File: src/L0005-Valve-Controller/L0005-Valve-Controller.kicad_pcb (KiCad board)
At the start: 4 copper layers, 141.7 x 50.5 mm, 100 parts, among them J1 Jumper_NO, J2 Jumper_NO, K1 AQH0223AX, K2 AQH0223AX, K3 AQH0223AX, K4 AQH0223AX, K5 AQH0223AX, K6 AQH0223AX, P1 3220-20-0200-00, P10 353620650, P11 353620650, P12 353620650, P13 353620650, P14 647676-3, P15 647676-3, P16 647676-2, P2 140-504-415-000, P3 647676-3, P4 647676-3, P5 647676-3, P6 647676-3, P7 647676-3, P8 647676-3, P9 647676-2, U1 LPC54113J256BD64QL, U2 LMS8117AMP-3.3_NOPB, U3 MAX3370EXK+T, U4 MAX3370EXK+T, U5 Optocoupler

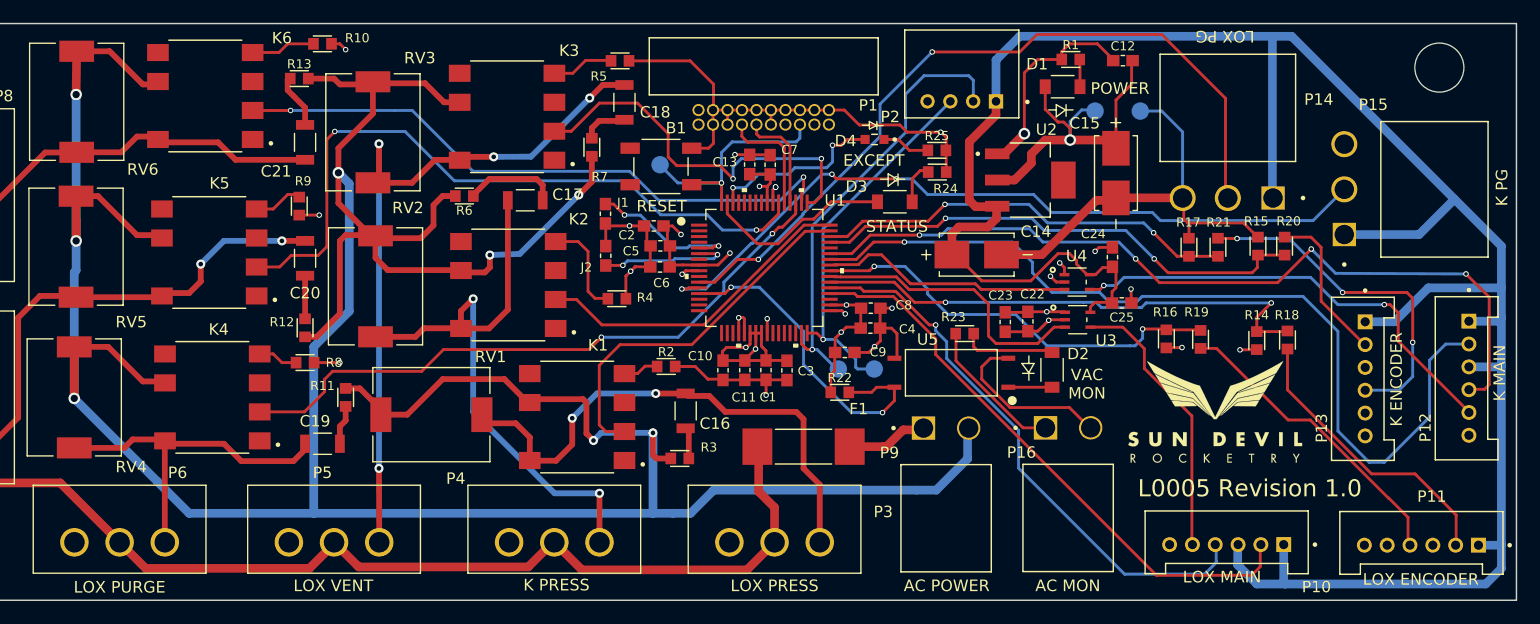
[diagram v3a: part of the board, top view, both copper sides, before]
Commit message: rerouted PCB to include 5V logic MOSFETS
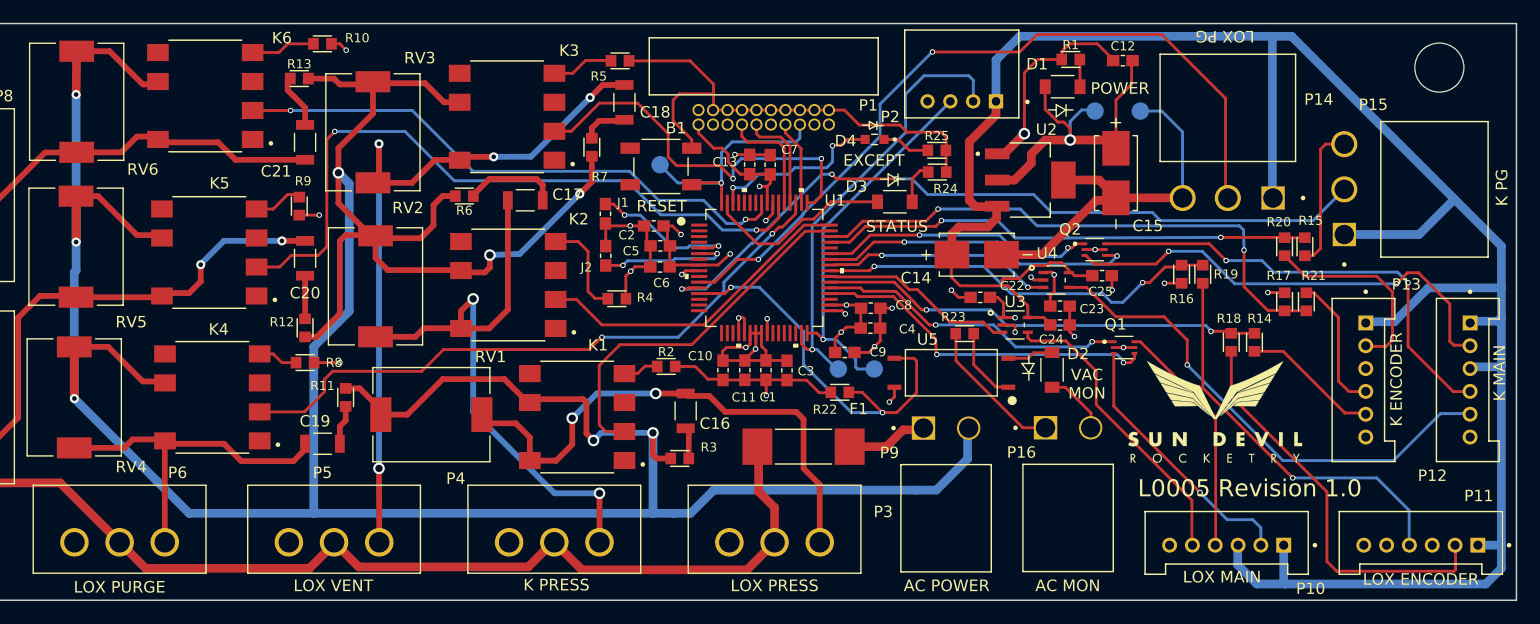
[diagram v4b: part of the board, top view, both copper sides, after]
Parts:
- added Q1: CMLDM7003, L0005-Valve-Controller:CMLDM7003 TR, F.Cu at (164.2, 105.4)
- added Q2: CMLDM7003, L0005-Valve-Controller:CMLDM7003 TR, F.Cu at (161.7, 96.8)
- B1: value PTS647SM38SMTR2LFS -> SW_PTS647SM38SMTR2LFS_CNK
- C14, C15: footprint Engine-Controller:CWR11HH106KB -> L0005-Valve-Controller:CWR11HH106KB
- LOGO1: value Logo -> LOGO
- U1: value LPC54113J256BD64QL -> LQFP64_10X10_NXP
- moved R17 9.65 mm to (178.3, 101.3)
- moved R21 9.10 mm to (180.2, 101.3)
- moved C24 7.51 mm to (158.6, 103.4), turned to 180 degrees
- moved R16 5.82 mm to (169.3, 98.9)
- moved R19 5.72 mm to (171.1, 98.9)
- moved U3 5.51 mm to (154.7, 103.4)
- moved C23 5.00 mm to (158.6, 101.7), turned to 180 degrees
- moved R18 4.93 mm to (173.6, 104.9)
- moved C22 4.67 mm to (151.6, 101.0), turned to 0 degrees
- moved R15 4.12 mm to (180.1, 96.5), turned to -90 degrees
- moved C25 2.95 mm to (162.3, 99.1)
- moved U4 1.85 mm to (158.3, 99.4)
- moved R14 0.25 mm to (175.7, 104.9)
- moved P12 0.18 mm to (194.6, 108.2)
- moved P13 0.11 mm to (185.4, 108.2)
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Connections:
- net /SBV1_PUL5 renamed /Valves/SBV1_PUL5
- net /SBV2_PUL5 renamed /Valves/SBV2_PUL5
- B1 pad 2: Net-(B1-Pad2) -> unconnected-(B1-Pad2)
- B1 pad 4: Net-(B1-Pad4) -> unconnected-(B1-Pad4)
- K1 pad 1: Net-(K1-Pad1) -> unconnected-(K1-Pad1)
- K1 pad 3: Net-(K1-Pad3) -> unconnected-(K1-Pad3)
- K1 pad 5: Net-(K1-Pad5) -> unconnected-(K1-Pad5)
- K2 pad 1: Net-(K2-Pad1) -> unconnected-(K2-Pad1)
- K2 pad 3: Net-(K2-Pad3) -> unconnected-(K2-Pad3)
- K2 pad 5: Net-(K2-Pad5) -> unconnected-(K2-Pad5)
- K3 pad 1: Net-(K3-Pad1) -> unconnected-(K3-Pad1)
- K3 pad 3: Net-(K3-Pad3) -> unconnected-(K3-Pad3)
- K3 pad 5: Net-(K3-Pad5) -> unconnected-(K3-Pad5)
- K4 pad 1: Net-(K4-Pad1) -> unconnected-(K4-Pad1)
- K4 pad 3: Net-(K4-Pad3) -> unconnected-(K4-Pad3)
- K4 pad 5: Net-(K4-Pad5) -> unconnected-(K4-Pad5)
- K5 pad 1: Net-(K5-Pad1) -> unconnected-(K5-Pad1)
- K5 pad 3: Net-(K5-Pad3) -> unconnected-(K5-Pad3)
- K5 pad 5: Net-(K5-Pad5) -> unconnected-(K5-Pad5)
- K6 pad 1: Net-(K6-Pad1) -> unconnected-(K6-Pad1)
- K6 pad 3: Net-(K6-Pad3) -> unconnected-(K6-Pad3)
- K6 pad 5: Net-(K6-Pad5) -> unconnected-(K6-Pad5)
- P1 pad 11: Earth -> unconnected-(P1-Pad11)
- P1 pad 13: Net-(P1-Pad13) -> SWO
- P1 pad 17: Net-(P1-Pad17) -> unconnected-(P1-Pad17)
- P1 pad 19: Net-(P1-Pad19) -> unconnected-(P1-Pad19)
- P1 pad 2: 3.3V -> unconnected-(P1-Pad2)
- P1 pad 3: Earth -> unconnected-(P1-Pad3)
- P1 pad 5: Earth -> unconnected-(P1-Pad5)
- P10 pad 2: ~{SBV1_EN} -> Net-(P10-Pad2)
- P10 pad 4: ~{SBV1_DIR} -> Net-(P10-Pad4)
- P12 pad 2: ~{SBV2_EN} -> Net-(P12-Pad2)
- P12 pad 4: ~{SBV2_DIR} -> Net-(P12-Pad4)
- P16 pad 2: Net-(P16-Pad2) -> Net-(D2-Pad1)
- P3 pad 3: Net-(P3-Pad3) -> unconnected-(P3-Pad3)
- P4 pad 3: Net-(P4-Pad3) -> unconnected-(P4-Pad3)
- P5 pad 3: Net-(P5-Pad3) -> unconnected-(P5-Pad3)
- P6 pad 3: Net-(P6-Pad3) -> unconnected-(P6-Pad3)
- P7 pad 3: Net-(P7-Pad3) -> unconnected-(P7-Pad3)
- P8 pad 3: Net-(P8-Pad3) -> unconnected-(P8-Pad3)
- R22 pad 1: 3.3V -> VAC_MON
- R22 pad 2: VAC_MON -> Earth
- R23 pad 1: Net-(D2-Pad2) -> Net-(R23-Pad1)
- U1 pad 1: Net-(U1-Pad1) -> unconnected-(U1-Pad1)
- U1 pad 10: Net-(U1-Pad10) -> unconnected-(U1-Pad10)
- U1 pad 14: Net-(U1-Pad14) -> unconnected-(U1-Pad14)
- U1 pad 15: Net-(U1-Pad15) -> unconnected-(U1-Pad15)
- U1 pad 16: Net-(U1-Pad16) -> unconnected-(U1-Pad16)
- U1 pad 17: Net-(U1-Pad17) -> unconnected-(U1-Pad17)
- U1 pad 18: Net-(U1-Pad18) -> unconnected-(U1-Pad18)
- U1 pad 19: Net-(U1-Pad19) -> unconnected-(U1-Pad19)
- U1 pad 2: Net-(U1-Pad2) -> unconnected-(U1-Pad2)
- U1 pad 26: Net-(U1-Pad26) -> unconnected-(U1-Pad26)
- U1 pad 27: Net-(U1-Pad27) -> unconnected-(U1-Pad27)
- U1 pad 28: Net-(U1-Pad28) -> unconnected-(U1-Pad28)
- U1 pad 29: Net-(U1-Pad29) -> unconnected-(U1-Pad29)
- U1 pad 3: Net-(U1-Pad3) -> unconnected-(U1-Pad3)
- U1 pad 30: Net-(U1-Pad30) -> unconnected-(U1-Pad30)
- U1 pad 35: Net-(U1-Pad35) -> unconnected-(U1-Pad35)
- U1 pad 36: ~{SBV1_EN} -> SBV1_EN
- U1 pad 37: ~{SBV1_DIR} -> SBV1_DIR
- U1 pad 4: Net-(U1-Pad4) -> unconnected-(U1-Pad4)
- U1 pad 42: ~{SBV2_EN} -> SBV2_EN
- U1 pad 43: ~{SBV2_DIR} -> SBV2_DIR
- U1 pad 44: Net-(U1-Pad44) -> unconnected-(U1-Pad44)
- U1 pad 50: SOL4 -> SWO
- U1 pad 57: Net-(U1-Pad57) -> SOL4
- U1 pad 58: Net-(U1-Pad58) -> unconnected-(U1-Pad58)
- U1 pad 59: Net-(U1-Pad59) -> unconnected-(U1-Pad59)
- U1 pad 60: Net-(U1-Pad60) -> unconnected-(U1-Pad60)
- U1 pad 61: Net-(U1-Pad61) -> unconnected-(U1-Pad61)
- U1 pad 7: Net-(U1-Pad7) -> unconnected-(U1-Pad7)
- U5 pad 1: Net-(D2-Pad1) -> Net-(R23-Pad1)
- U5 pad 2: Net-(P16-Pad2) -> Net-(D2-Pad2)
- U5 pad 3: Earth -> VAC_MON
- U5 pad 4: VAC_MON -> 3.3V
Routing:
- net ~{SBV2_EN}: track 78.1 -> 0.00 mm, vias 1 -> 0
- net ~{SBV2_DIR}: track 73.4 -> 0.00 mm, vias 4 -> 0
- net ~{SBV1_EN}: track 51.1 -> 0.00 mm
- net ~{SBV1_DIR}: track 49.7 -> 0.00 mm, vias 1 -> 0
- net Net-(P12-Pad4): track 0.00 -> 40.8 mm, vias 0 -> 2
- net Net-(P12-Pad2): track 0.00 -> 40.6 mm, vias 0 -> 2
- net SBV1_EN: track 0.00 -> 30.6 mm, vias 0 -> 2
- net SBV2_EN: track 0.00 -> 28.0 mm, vias 0 -> 2
- net SBV1_DIR: track 0.00 -> 27.2 mm, vias 0 -> 2
- net SBV2_DIR: track 0.00 -> 24.3 mm, vias 0 -> 2
- net Earth: track 165.5 -> 189.4 mm, vias 23 -> 24
- net Net-(P10-Pad2): track 0.00 -> 23.4 mm, vias 0 -> 1
- net Net-(P10-Pad4): track 0.00 -> 21.1 mm
- net Net-(P13-Pad4): track 30.8 -> 12.1 mm, vias 3 -> 0
- net Net-(P16-Pad2): track 15.2 -> 0.00 mm
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
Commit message: produced gerbers files
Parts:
- C14, C15: footprint L0005-Valve-Controller:CWR11HH106KB -> L0005-Valve-Controller:T491A106K010AT
- LOGO1: value LOGO -> Logo
- U1: value LQFP64_10X10_NXP -> LPC54113J256BD64QL

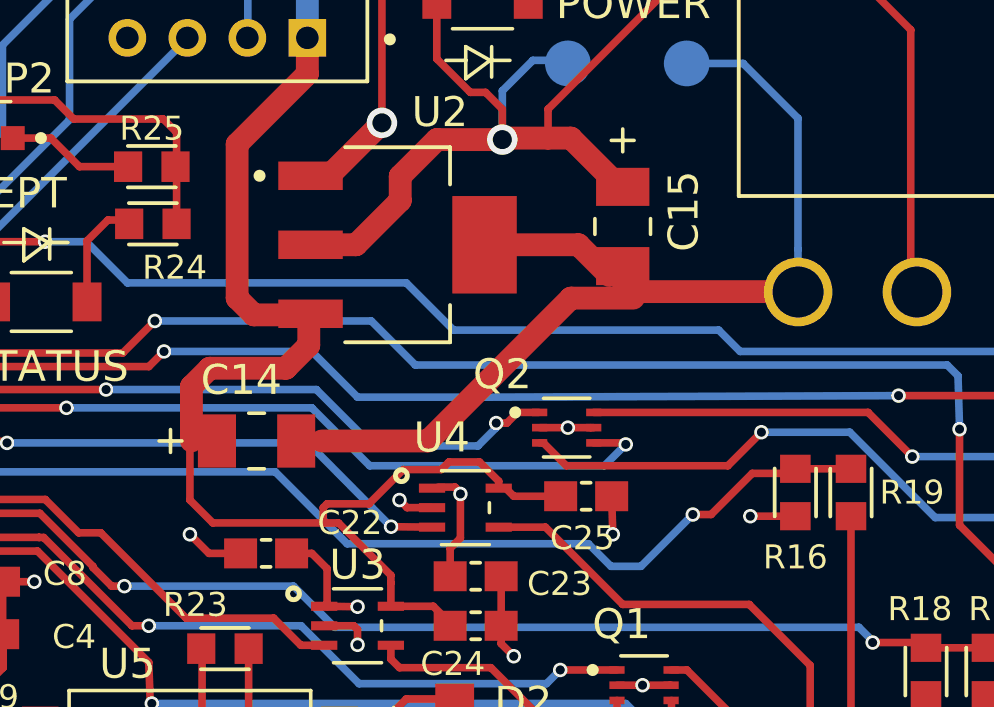
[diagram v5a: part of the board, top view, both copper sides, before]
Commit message: Fixed error with regulator routimg
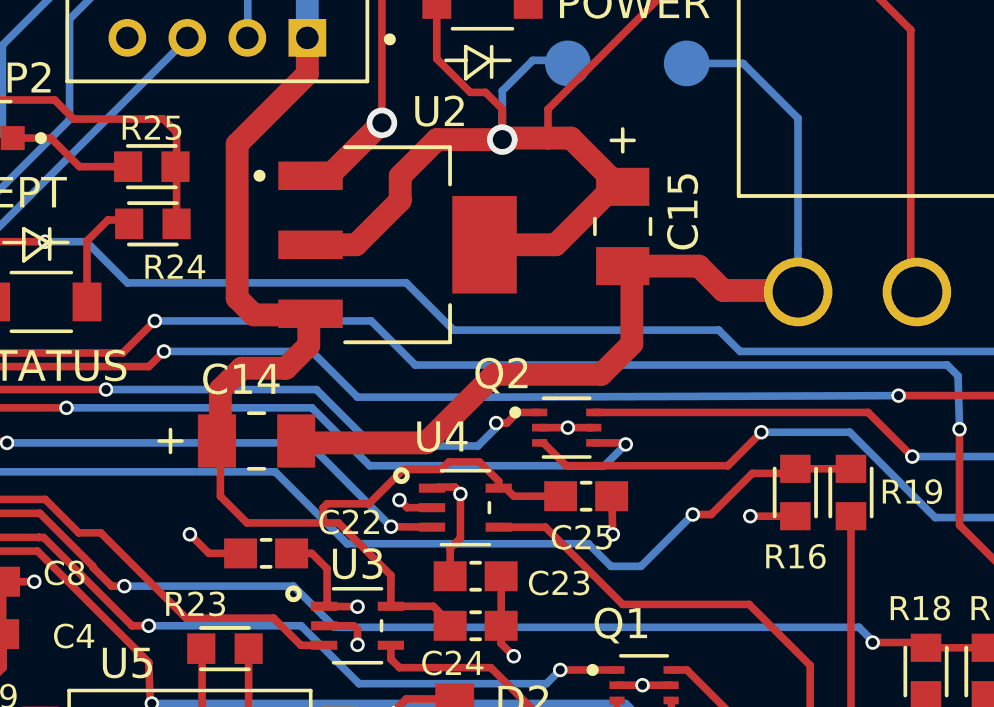
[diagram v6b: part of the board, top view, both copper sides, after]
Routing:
- net 3.3V: track 87.9 -> 92.8 mm
- net 5V: track 201.4 -> 199.2 mm
- net Earth: track 189.4 -> 187.5 mm

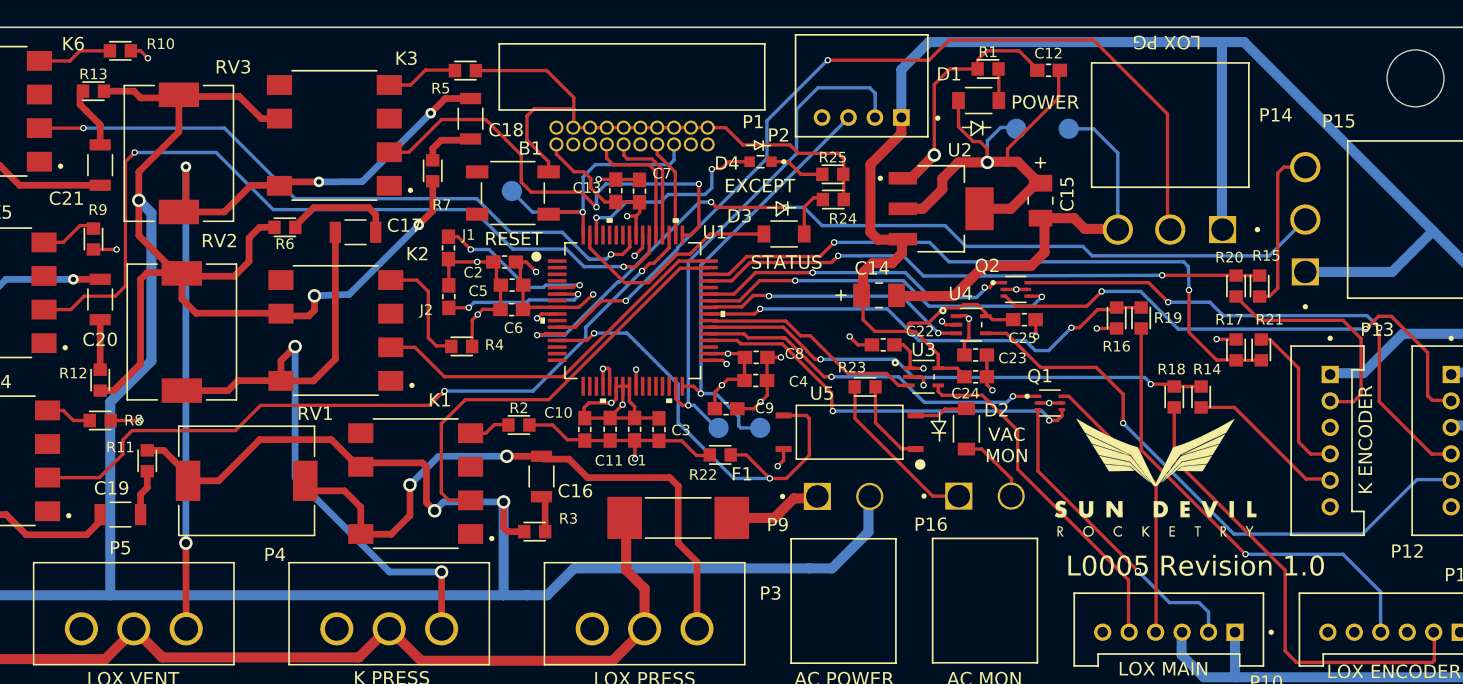
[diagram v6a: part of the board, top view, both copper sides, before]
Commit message: added new STM32 MCU to lib files
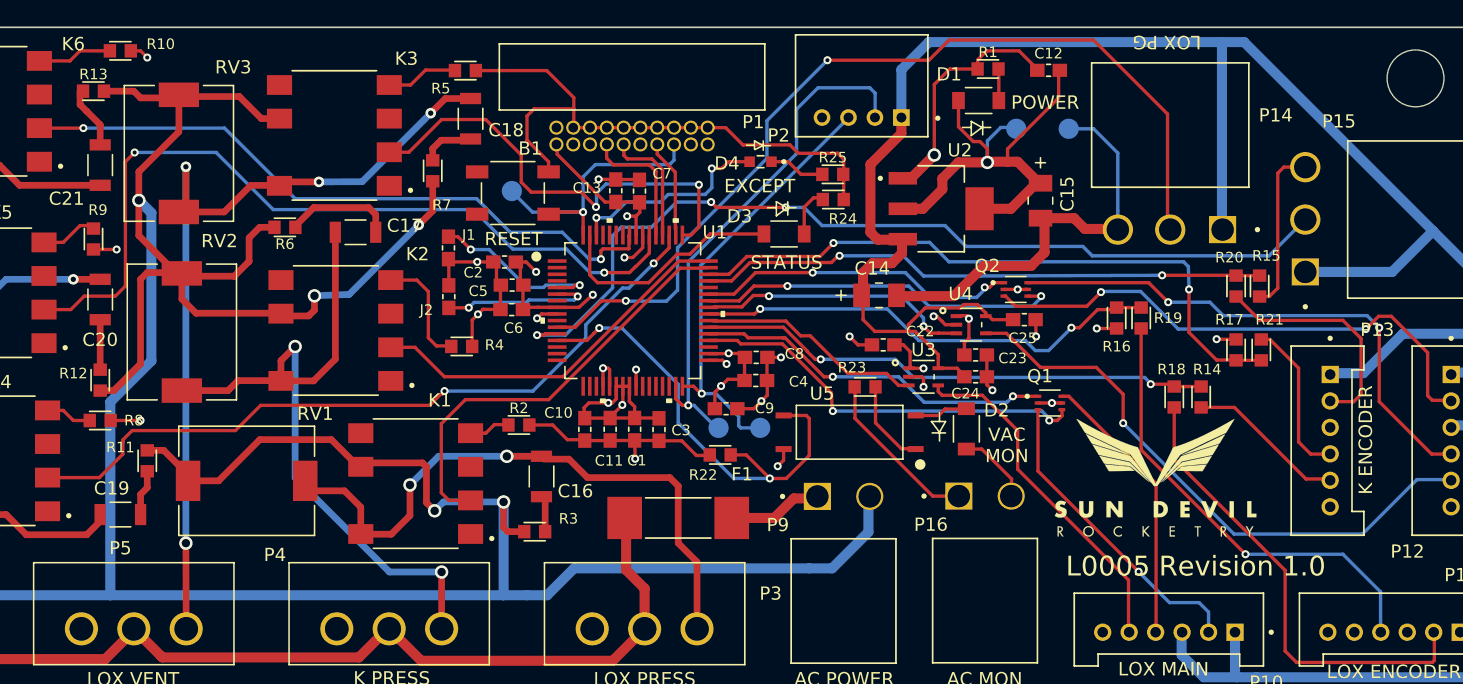
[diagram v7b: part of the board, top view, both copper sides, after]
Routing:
- net PG2: track 66.6 -> 68.9 mm
- net PG1: track 67.9 -> 69.7 mm
- net Earth: track 187.5 -> 189.1 mm
- net STATUS: track 16.8 -> 18.0 mm
- net SOL4: track 49.6 -> 50.4 mm
- net 3.3V: track 92.8 -> 92.2 mm
